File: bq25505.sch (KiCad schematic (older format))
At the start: 26 parts

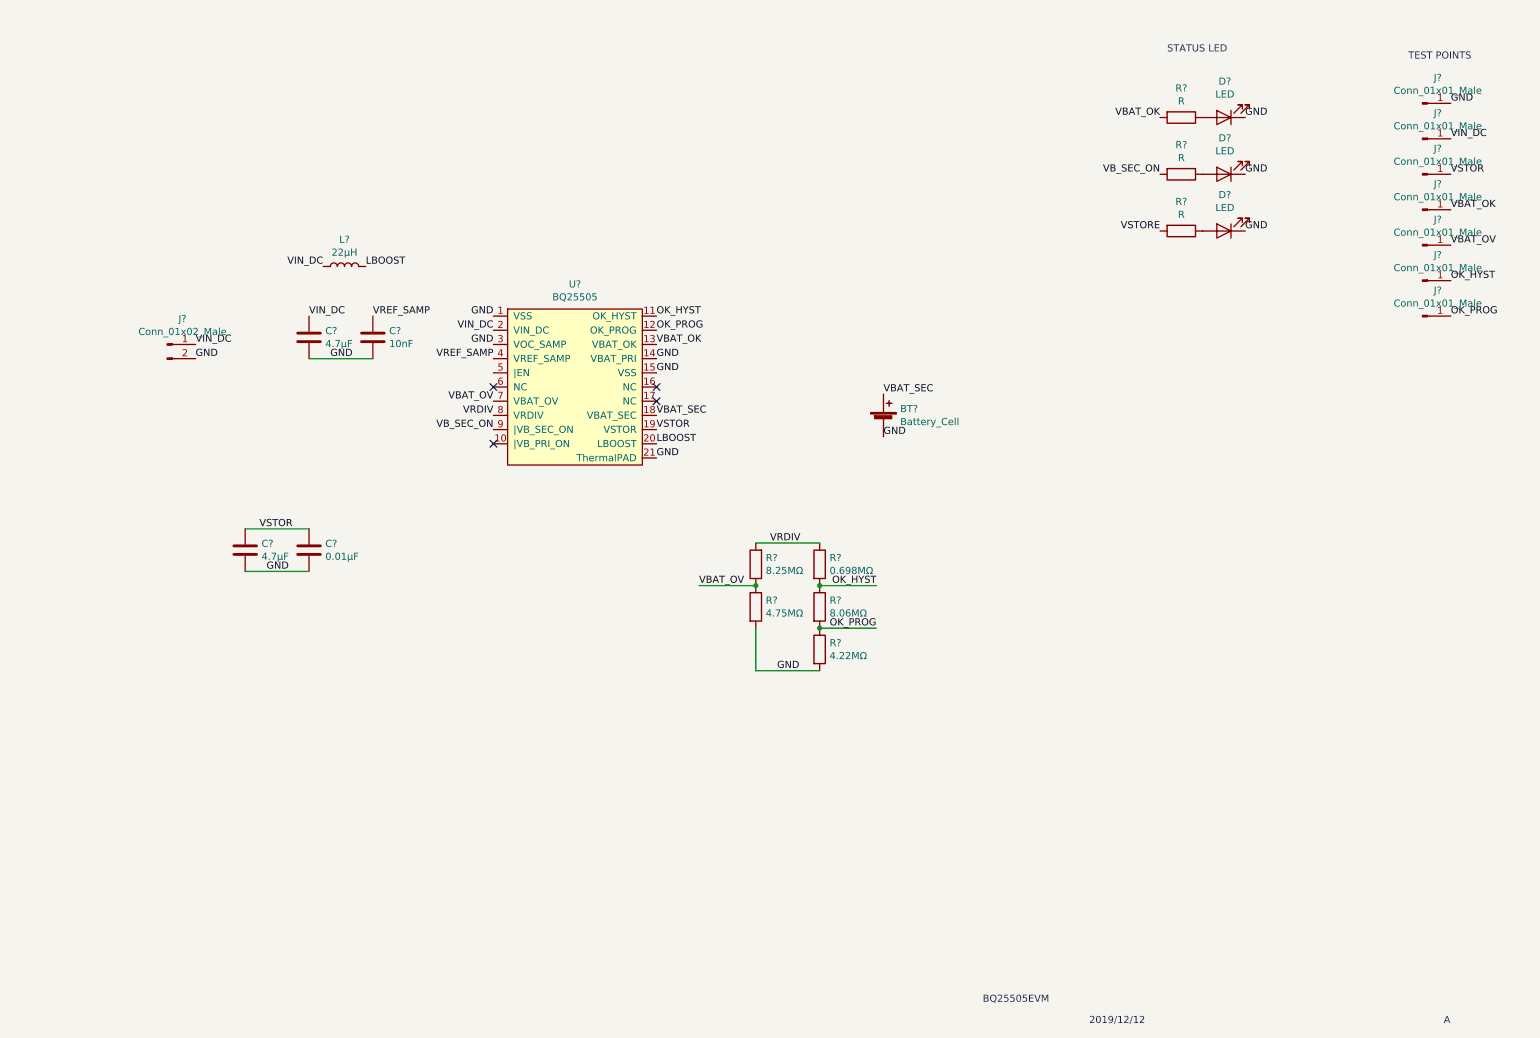
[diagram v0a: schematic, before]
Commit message: Rearranged some elements on the schematic file
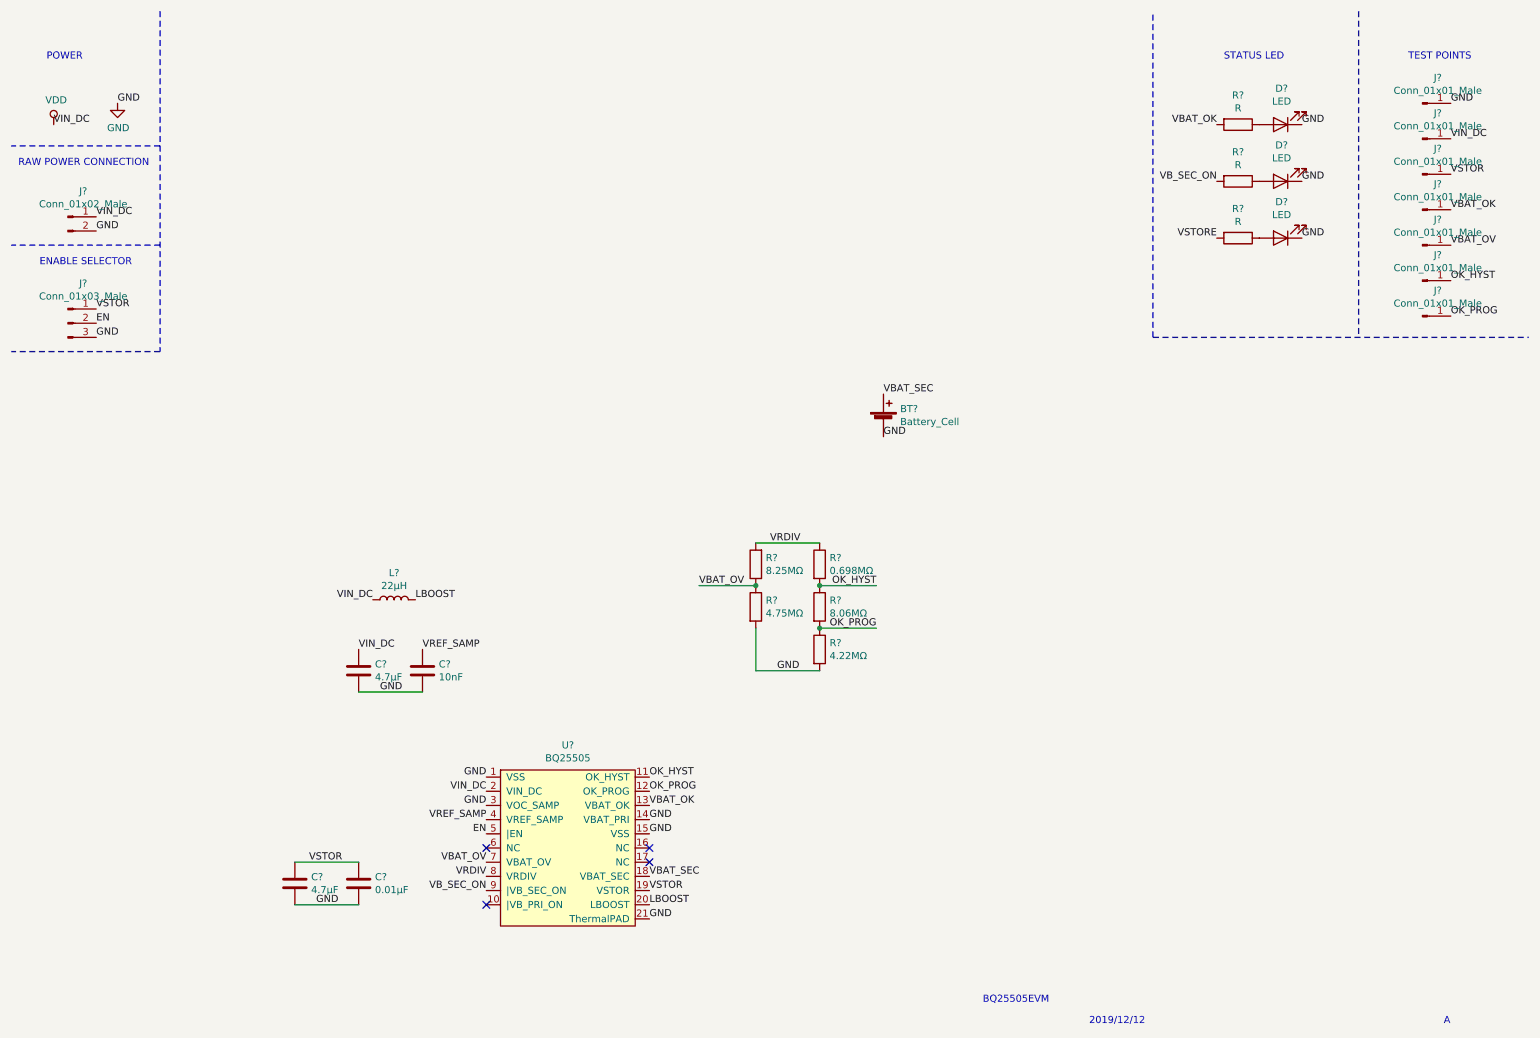
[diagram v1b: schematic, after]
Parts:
- added J?: Conn_01x03_Male, symbol Connector:Conn_01x03_Male
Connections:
- net GND: now also J?.3 (Pin_3)
- net VSTOR: now also J?.1 (Pin_1)
- net EN: now reaches U?.5 (|EN)
- net EN: now also J?.2 (Pin_2)
- net VIN_DC renamed VDD
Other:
- note added: "ENABLE SELECTOR"
- note added: "POWER"
- note added: "RAW POWER CONNECTION"
- moved on the sheet: C?, D?, J?, L?, R?, U?

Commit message: Added datasheets
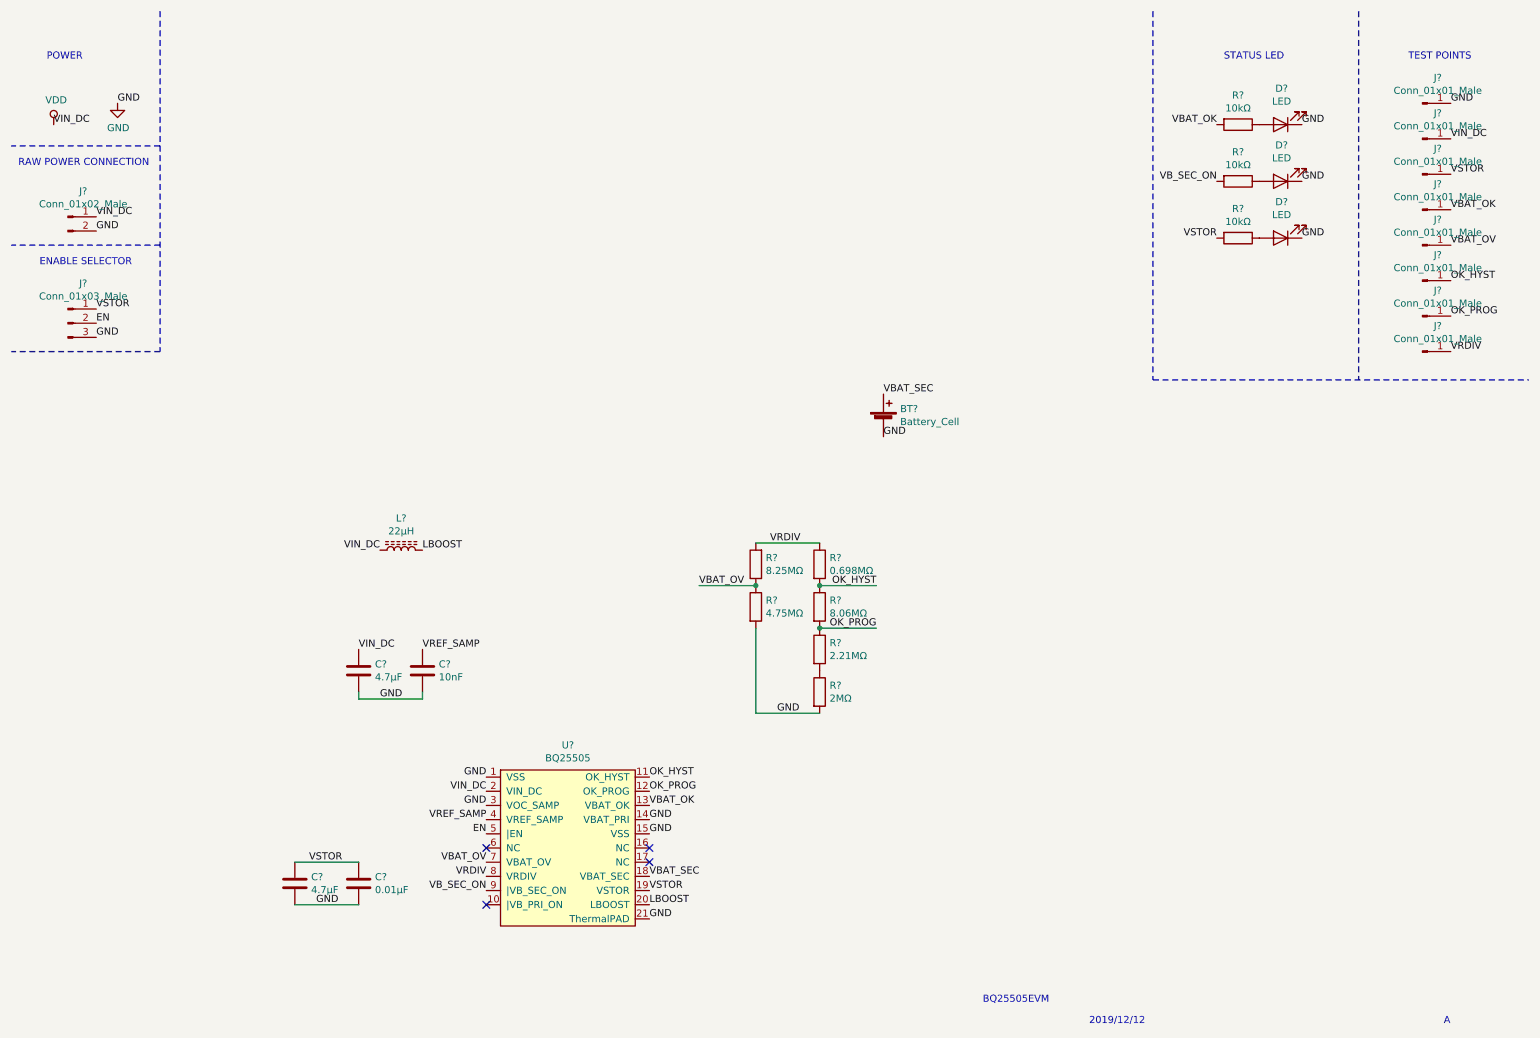
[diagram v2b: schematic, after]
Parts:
- removed L?: 22μH, symbol Device:L
- added J?: Conn_01x01_Male, Connector_PinHeader_1.27mm:PinHeader_1x01_P1.27mm_Vertical, symbol Connector:Conn_01x01_Male
- added L?: 22μH, Inductor_SMD:L_0805_2012Metric_Pad1.15x1.40mm_HandSolder, symbol Device:L_Core_Ferrite
- added R?: 2MΩ, Resistor_SMD:R_0805_2012Metric_Pad1.15x1.40mm_HandSolder, symbol Device:R
- BT?: footprint (none) -> Capacitor_THT:C_Radial_D12.5mm_H20.0mm_P5.00mm
- C? (x4): footprint (none) -> Capacitor_SMD:C_0805_2012Metric_Pad1.15x1.40mm_HandSolder
- D? (x3): footprint (none) -> LED_SMD:LED_0805_2012Metric_Pad1.15x1.40mm_HandSolder
- J?: footprint (none) -> Connector_PinHeader_1.27mm:PinHeader_1x03_P1.27mm_Vertical
- J?: footprint (none) -> Connector_PinHeader_1.27mm:PinHeader_1x02_P1.27mm_Vertical
- J? (x7): footprint (none) -> Connector_PinHeader_1.27mm:PinHeader_1x01_P1.27mm_Vertical
- R? (x4): footprint (none) -> Resistor_SMD:R_0805_2012Metric_Pad1.15x1.40mm_HandSolder
- R?: value 4.22MΩ -> 2.21MΩ; footprint (none) -> Resistor_SMD:R_0805_2012Metric_Pad1.15x1.40mm_HandSolder
- R? (x3): value R -> 10kΩ; footprint (none) -> Resistor_SMD:R_0805_2012Metric_Pad1.15x1.40mm_HandSolder
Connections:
- net VSTORE is gone; now on net VSTOR: R?.2
- net GND: now also R?.2; no longer R?.2
- net LBOOST: now also L?.2
- net VDD: now also L?.1
- net VRDIV: now also J?.1 (Pin_1)
- new net: R?.1, R?.2

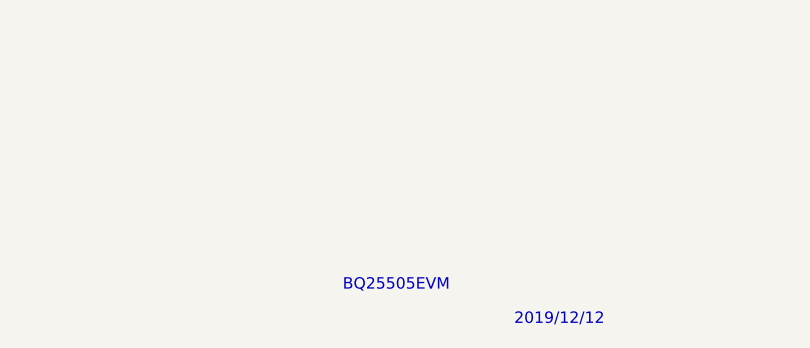
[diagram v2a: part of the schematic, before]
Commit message: It's not a BQ25505, it's a BQ25570
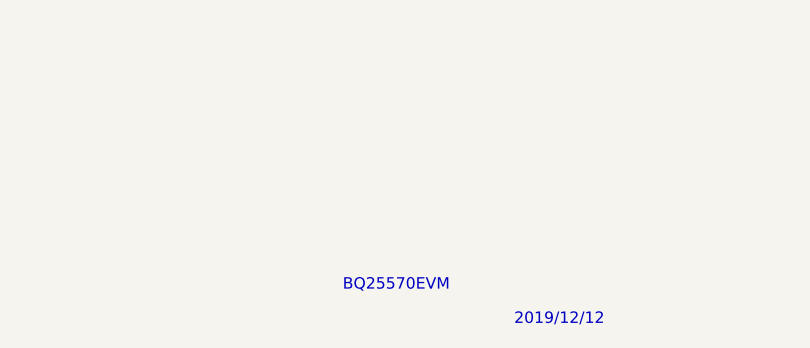
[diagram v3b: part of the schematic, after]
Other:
- note added: "BQ25570EVM"
- note removed: "BQ25505EVM"
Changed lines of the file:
@@
 TEST POINTS
 Text Notes 7350 7500 0    50   ~ 0
-BQ25505EVM
+BQ25570EVM
 Text Notes 8100 7650 0    50   ~ 0
 2019/12/12
